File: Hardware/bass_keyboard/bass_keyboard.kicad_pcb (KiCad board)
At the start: 2 copper layers, 291.3 x 154.8 mm, 188 parts, among them J1 Conn_02x17_Top_Bottom

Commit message: Silkscreen labels
Added model, part name, logo
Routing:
- net (no net): track 0.00 -> 110.5 mm
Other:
- board text added: "Synharmonium Bass Keyboard Protoyping Master rev 0.1"
- board text added: "UIW"

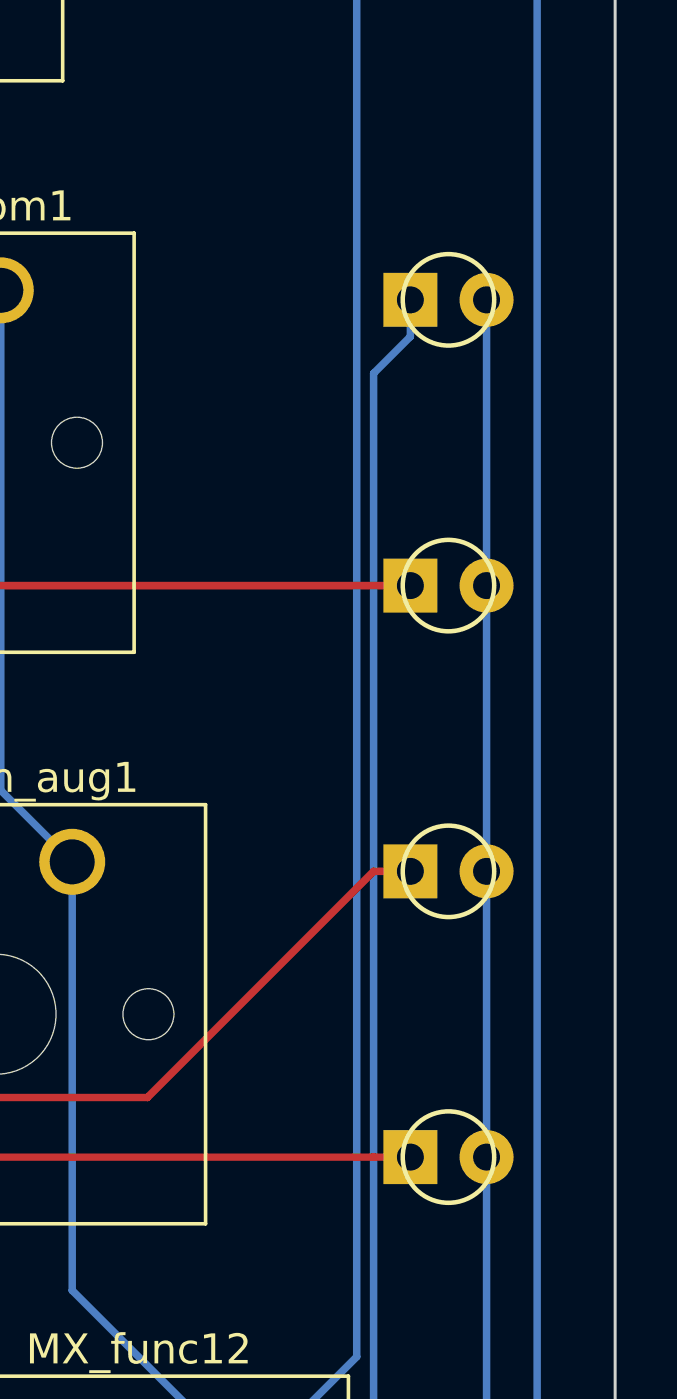
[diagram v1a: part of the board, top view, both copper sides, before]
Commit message: Renders
Replaced componentless led footprint with componentfull footprint. Rendered PCB with raytracing at a few angles.
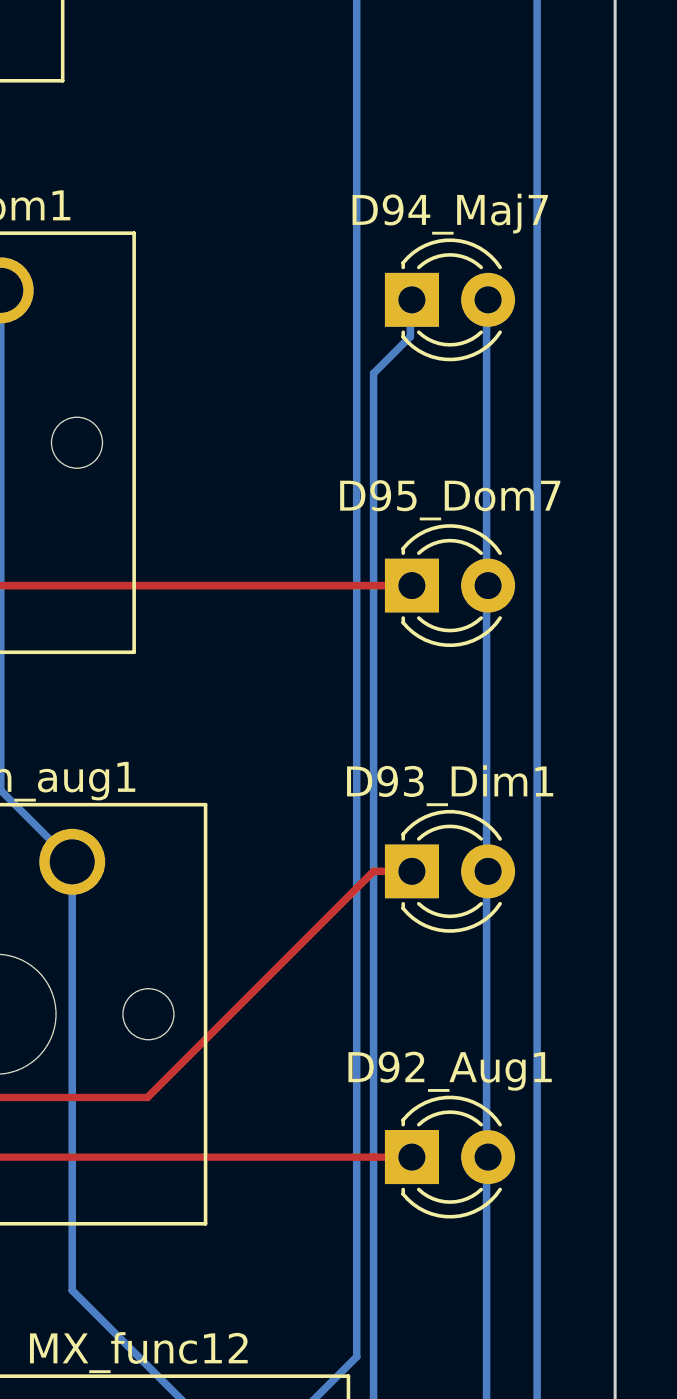
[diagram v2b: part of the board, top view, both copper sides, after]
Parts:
- D92_Aug1, D93_Dim1, D94_Maj7, D95_Dom7: footprint random-keyboard-parts:LED_D3.0mm-Pretty -> LED_THT:LED_D3.0mm
- moved D92_Aug1 1.22 mm to (310.7, 192.9)
- moved D93_Dim1 1.22 mm to (310.7, 183.4)
- moved D94_Maj7 1.22 mm to (310.7, 164.3)
- moved D95_Dom7 1.22 mm to (310.7, 173.8)
